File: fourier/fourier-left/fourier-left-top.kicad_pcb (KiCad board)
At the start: 2 copper layers, 136.6 x 92.2 mm, 7 parts

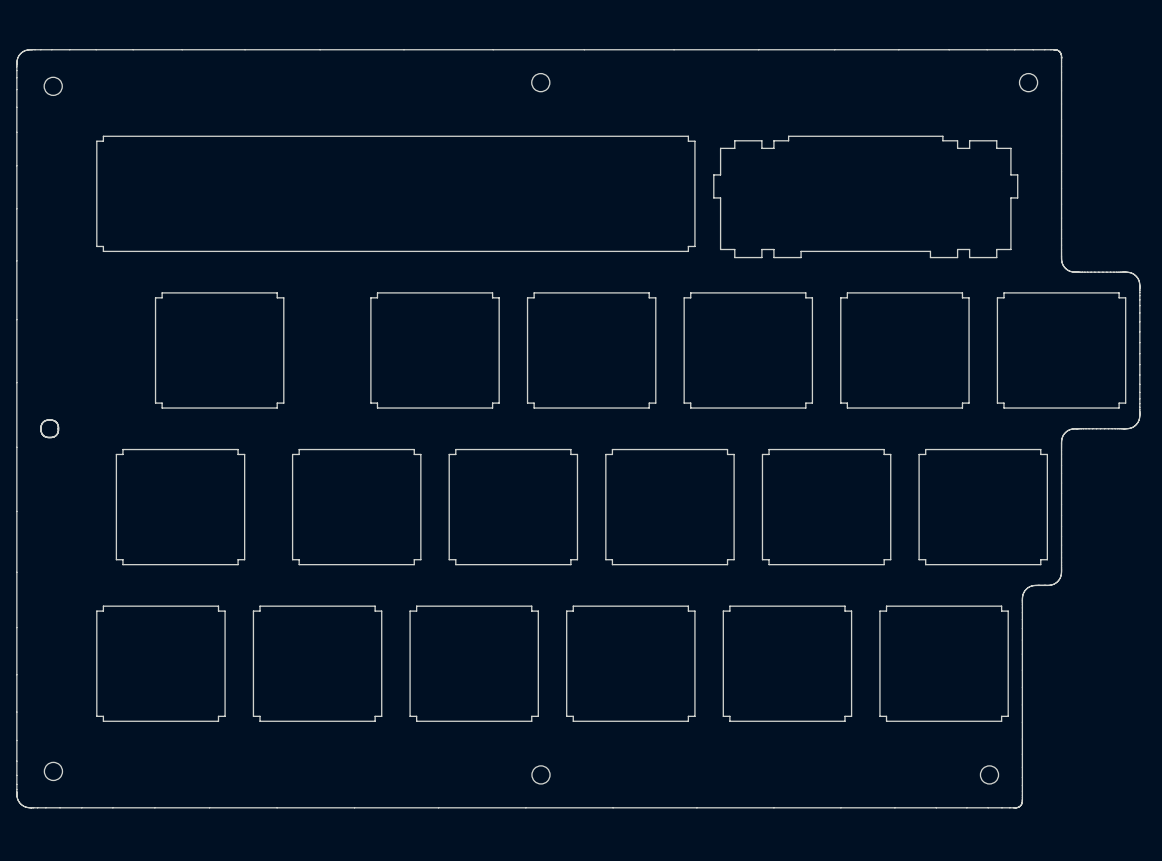
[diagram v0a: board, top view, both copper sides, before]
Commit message: Top height and center hole adjusment
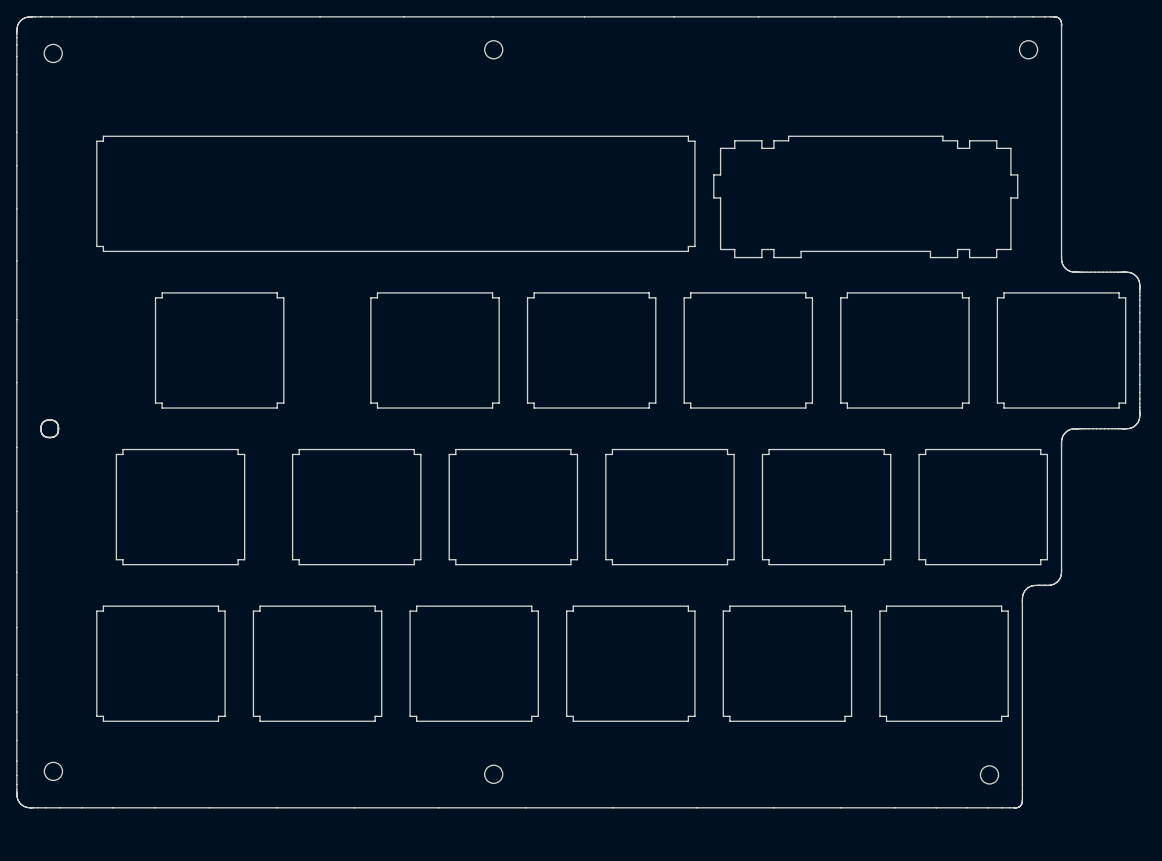
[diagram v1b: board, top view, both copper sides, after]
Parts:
- moved REF** 6.98 mm to (78.0, 22.9)
- moved REF** 5.75 mm to (78.0, 111.0)
- moved REF** 4.00 mm to (143.1, 22.9)
- moved REF** 4.00 mm to (24.4, 23.3)
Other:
- board size 136.6 x 92.2 mm -> 136.6 x 96.2 mm

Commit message: rotate left-top and update to KiCad 5.99
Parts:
- removed the REF** at (78.0, 111.0)
- removed the REF** at (138.3, 111.1)
- removed the REF** at (143.1, 22.9)
- removed the REF** at (78.0, 22.9)
- removed the REF** at (24.4, 23.3)
- removed the REF** at (24.0, 69.0)
- removed the REF** at (24.4, 110.7)
- added REF**: MountingHole_2.2mm_M2, Mounting_Holes:MountingHole_2.2mm_M2, F.Cu at (138.9, 27.5)
- added REF**: MountingHole_2.2mm_M2, Mounting_Holes:MountingHole_2.2mm_M2, F.Cu at (25.1, 27.9)
- added REF**: MountingHole_2.2mm_M2, Mounting_Holes:MountingHole_2.2mm_M2, F.Cu at (25.0, 115.0)
- added REF**: MountingHole_2.2mm_M2, Mounting_Holes:MountingHole_2.2mm_M2, F.Cu at (24.6, 73.4)
- added REF**: MountingHole_2.2mm_M2, Mounting_Holes:MountingHole_2.2mm_M2, F.Cu at (143.7, 115.5)
- added REF**: MountingHole_2.2mm_M2, Mounting_Holes:MountingHole_2.2mm_M2, F.Cu at (84.4, 27.5)
- added REF**: MountingHole_2.2mm_M2, Mounting_Holes:MountingHole_2.2mm_M2, F.Cu at (84.3, 115.5)
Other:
- board size 136.6 x 96.2 mm -> 136.6 x 96 mm
- net class Default removed

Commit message: removed center holes
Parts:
- removed the REF** at (84.4, 27.5)
- removed the REF** at (84.3, 115.5)
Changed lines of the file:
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@@
-    (pad "" np_thru_hole circle locked (at 0 0) (size 2.2 2.2) (drill 2.2) (layers *.Cu *.Mask))
-  )
-  (footprint "Mounting_Holes:MountingHole_2.2mm_M2" (layer "F.Cu")
-    (at 84.353268 27.48495)
-    (descr "Mounting Hole 2.2mm, no annular, M2")
-    (tags "mounting hole 2.2mm no annular m2")
-    (attr exclude_from_pos_files exclude_from_bom)
-    (fp_text reference "REF**" (at 0 -3.2) (layer "F.SilkS") hide
-      (effects (font (size 1 1) (thickness 0.15)))
-    )
-    (fp_text value "MountingHole_2.2mm_M2" (at 0 3.2) (layer "F.Fab") hide
-      (effects (font (size 1 1) (thickness 0.15)))
-    )
-    (fp_text user "${REFERENCE}" (at 0.3 0) (layer "F.Fab")
-      (effects (font (size 1 1) (thickness 0.15)))
-    )
-    (fp_circle (center 0 0) (end 2.2 0) (layer "Cmts.User") (width 0.15) (fill none))
-    (fp_circle (center 0 0) (end 2.45 0) (layer "F.CrtYd") (width 0.05) (fill none))
-    (pad "" np_thru_hole circle locked (at 0 0) (size 2.2 2.2) (drill 2.2) (layers *.Cu *.Mask))
-  )
-  (footprint "Mounting_Holes:MountingHole_2.2mm_M2" (layer "F.Cu")
-    (at 84.328268 115.471903)
-    (descr "Mounting Hole 2.2mm, no annular, M2")
-    (tags "mounting hole 2.2mm no annular m2")
-    (attr exclude_from_pos_files exclude_from_bom)
-    (fp_text reference "REF**" (at 0 -3.2) (layer "F.SilkS") hide
-      (effects (font (size 1 1) (thickness 0.15)))
-    )
-    (fp_text value "MountingHole_2.2mm_M2" (at 0 3.2) (layer "F.Fab") hide
-      (effects (font (size 1 1) (thickness 0.15)))
-    )
-    (fp_text user "${REFERENCE}" (at 0.3 0) (layer "F.Fab")
-      (effects (font (size 1 1) (thickness 0.15)))
-    )
-    (fp_circle (center 0 0) (end 2.2 0) (layer "Cmts.User") (width 0.15) (fill none))
-    (fp_circle (center 0 0) (end 2.45 0) (layer "F.CrtYd") (width 0.05) (fill none))
     (pad "" np_thru_hole circle locked (at 0 0) (size 2.2 2.2) (drill 2.2) (layers *.Cu *.Mask))
   )
